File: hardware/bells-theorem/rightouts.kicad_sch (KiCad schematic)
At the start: 54 parts, among them U4 TL074, U5 TL074, U6 TL074, U7 TL072

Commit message: Modified with Jim M's recommendations for input scaling
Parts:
- C10, C11, C12, C13, C7, C8, C9: value 15nF -> 1nF
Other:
- note added: "PWM single pole RC filters 10K + 1nF for 15KHz cutoff (PWM output at 146KHz)"
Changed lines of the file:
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@@
     (stroke (width 0) (type default) (color 0 0 0 0))
+  )
+  (text "PWM single pole RC filters\n10K + 1nF for 15KHz cutoff\n(PWM output at 146KHz)"
+    (at 151.13 90.805 0)
+    (effects (font (size 1.27 1.27)) (justify left bottom))
   )
   (hierarchical_label "ABC_in" (shape input) (at 59.69 77.47 180)
@@
       (effects (font (size 1.27 1.27)) (justify left))
     )
-    (property "Value" "15nF" (id 1) (at 78.74 167.64 90)
+    (property "Value" "1nF" (id 1) (at 78.74 167.64 90)
       (effects (font (size 1.27 1.27)) (justify left))
     )
@@
       (effects (font (size 1.27 1.27)) (justify left))
     )
-    (property "Value" "15nF" (id 1) (at 77.47 139.7 90)
+    (property "Value" "1nF" (id 1) (at 77.47 139.7 90)
       (effects (font (size 1.27 1.27)) (justify left))
     )
@@
       (effects (font (size 1.27 1.27)) (justify left))
     )
-    (property "Value" "15nF" (id 1) (at 76.2 115.57 90)
+    (property "Value" "1nF" (id 1) (at 76.2 115.57 90)
       (effects (font (size 1.27 1.27)) (justify left))
     )
@@
       (effects (font (size 1.27 1.27)) (justify left))
     )
-    (property "Value" "15nF" (id 1) (at 76.2 88.9 90)
+    (property "Value" "1nF" (id 1) (at 76.2 88.9 90)
       (effects (font (size 1.27 1.27)) (justify left))
     )
@@
       (effects (font (size 1.27 1.27)) (justify left))
     )
-    (property "Value" "15nF" (id 1) (at 74.93 63.5 90)
+    (property "Value" "1nF" (id 1) (at 74.93 63.5 90)
       (effects (font (size 1.27 1.27)) (justify left))
     )
@@
       (effects (font (size 1.27 1.27)) (justify left))
     )
-    (property "Value" "15nF" (id 1) (at 76.2 39.37 90)
+    (property "Value" "1nF" (id 1) (at 76.2 39.37 90)
       (effects (font (size 1.27 1.27)) (justify left))
     )
@@
       (effects (font (size 1.27 1.27)) (justify left))
     )
-    (property "Value" "15nF" (id 1) (at 74.93 13.97 90)
-      (effects (font (size 1.27 1.27)) (justify left))
-    )
+    (property "Value" "1nF" (id 1) (at 74.93 13.97 90)
+      (effects (font (size 1.27 1.27)) (justify left))
+    )

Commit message: All changes up to date with latest revisions
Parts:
- C10, C11, C12, C13, C14, C15, C16, C17, C18, C19, C20, C21, C7, C8, C9: footprint Capacitor_SMD:C_0805_2012Metric_Pad1.15x1.40mm_HandSolder -> Capacitor_SMD:C_0805_2012Metric_Pad1.18x1.45mm_HandSolder
- R11, R14, R17, R20, R23, R26, R29, R32, R35, R36, R37, R38, R39, R40, R41, R42, R43, R44, R45, R46, R47, R48, R49, R50, R51, R52, R53, R54, R55, R56, R57, R58, R59, R60, R61: footprint Resistor_SMD:R_0805_2012Metric_Pad1.15x1.40mm_HandSolder -> Resistor_SMD:R_0805_2012Metric_Pad1.20x1.40mm_HandSolder
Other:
- title: (none) -> Bell's Theorem

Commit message: last hardware / software updates
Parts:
- removed C15, C17, C19, C21: 100nF, Capacitor_SMD:C_0805_2012Metric_Pad1.18x1.45mm_HandSolder, symbol Device:C_Small
- added C62, C63, C64, C65, C66, C67, C68: 2n, Capacitor_SMD:C_0805_2012Metric_Pad1.18x1.45mm_HandSolder, symbol Device:C_Small
- C10, C11, C12, C13, C7, C8, C9: value 1nF -> 3.3n
- U4, U5, U6: symbol Amplifier_Operational:TL074 -> Amplifier_Operational:MCP6004
- U7: symbol Amplifier_Operational:TL072 -> Amplifier_Operational:MCP6002-xSN
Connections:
- net -12V is gone; now on net GND: U4.11 (V-), U5.11 (V-), U6.11 (V-), U7.4 (V-)
- net AB: now also C65.1
- net ABC: now also C66.1
- net ABCD: now also C68.1
- net B: now also C64.1
- net BC: now also C63.1
- net BCD: now also C67.1
- net C: now also C62.1
- net at R41.1, R48.2, U4.2 (-): now also C64.2
- net at R42.1, R51.2, U4.6 (-): now also C65.2
- net at R47.1, R54.2, U7.2 (-): now also C68.2
- net at R43.1, R49.2, U5.2 (-): now also C66.2
- net at R44.1, R52.2, U5.6 (-): now also C63.2
- net at R45.1, R50.2, U6.2 (-): now also C67.2
- net at R46.1, R53.2, U6.6 (-): now also C62.2
- net +12V renamed +10V
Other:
- note added: "symbols are changed but the freaking names are not"
- note removed: "PWM single pole RC filters 10K + 1nF for 15KHz cutoff (PWM output at 146KHz)"
- moved on the sheet: R14, R20, R26

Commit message: version 0.6 hardware and code
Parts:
- added C21, C35, C37, C39: 100nF, Capacitor_SMD:C_0805_2012Metric_Pad1.18x1.45mm_HandSolder, symbol Device:C_Small
- U4, U5, U6: value TL074 -> TLV9304; symbol Amplifier_Operational:MCP6004 -> Amplifier_Operational:TLC274
- U7: value TL072 -> TLV9302; symbol Amplifier_Operational:MCP6002-xSN -> Amplifier_Operational:TLC272
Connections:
- net GND: now also C21.2, C35.2, C37.2, C39.2; no longer U4.11 (V-), U5.11 (V-), U6.11 (V-), U7.4 (V-)
- new net -10V: C21.1, C35.1, C37.1, C39.1, U4.11 (V-), U5.11 (V-), U6.11 (V-), U7.4 (V-)
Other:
- note added: "Can't use 6004's they won't tolerate 10V operation"
- note added: "doing this architecture with single sided supplies is a lot more complicated than it might look. So using dual supply."
- note removed: "symbols are changed but the freaking names are not"

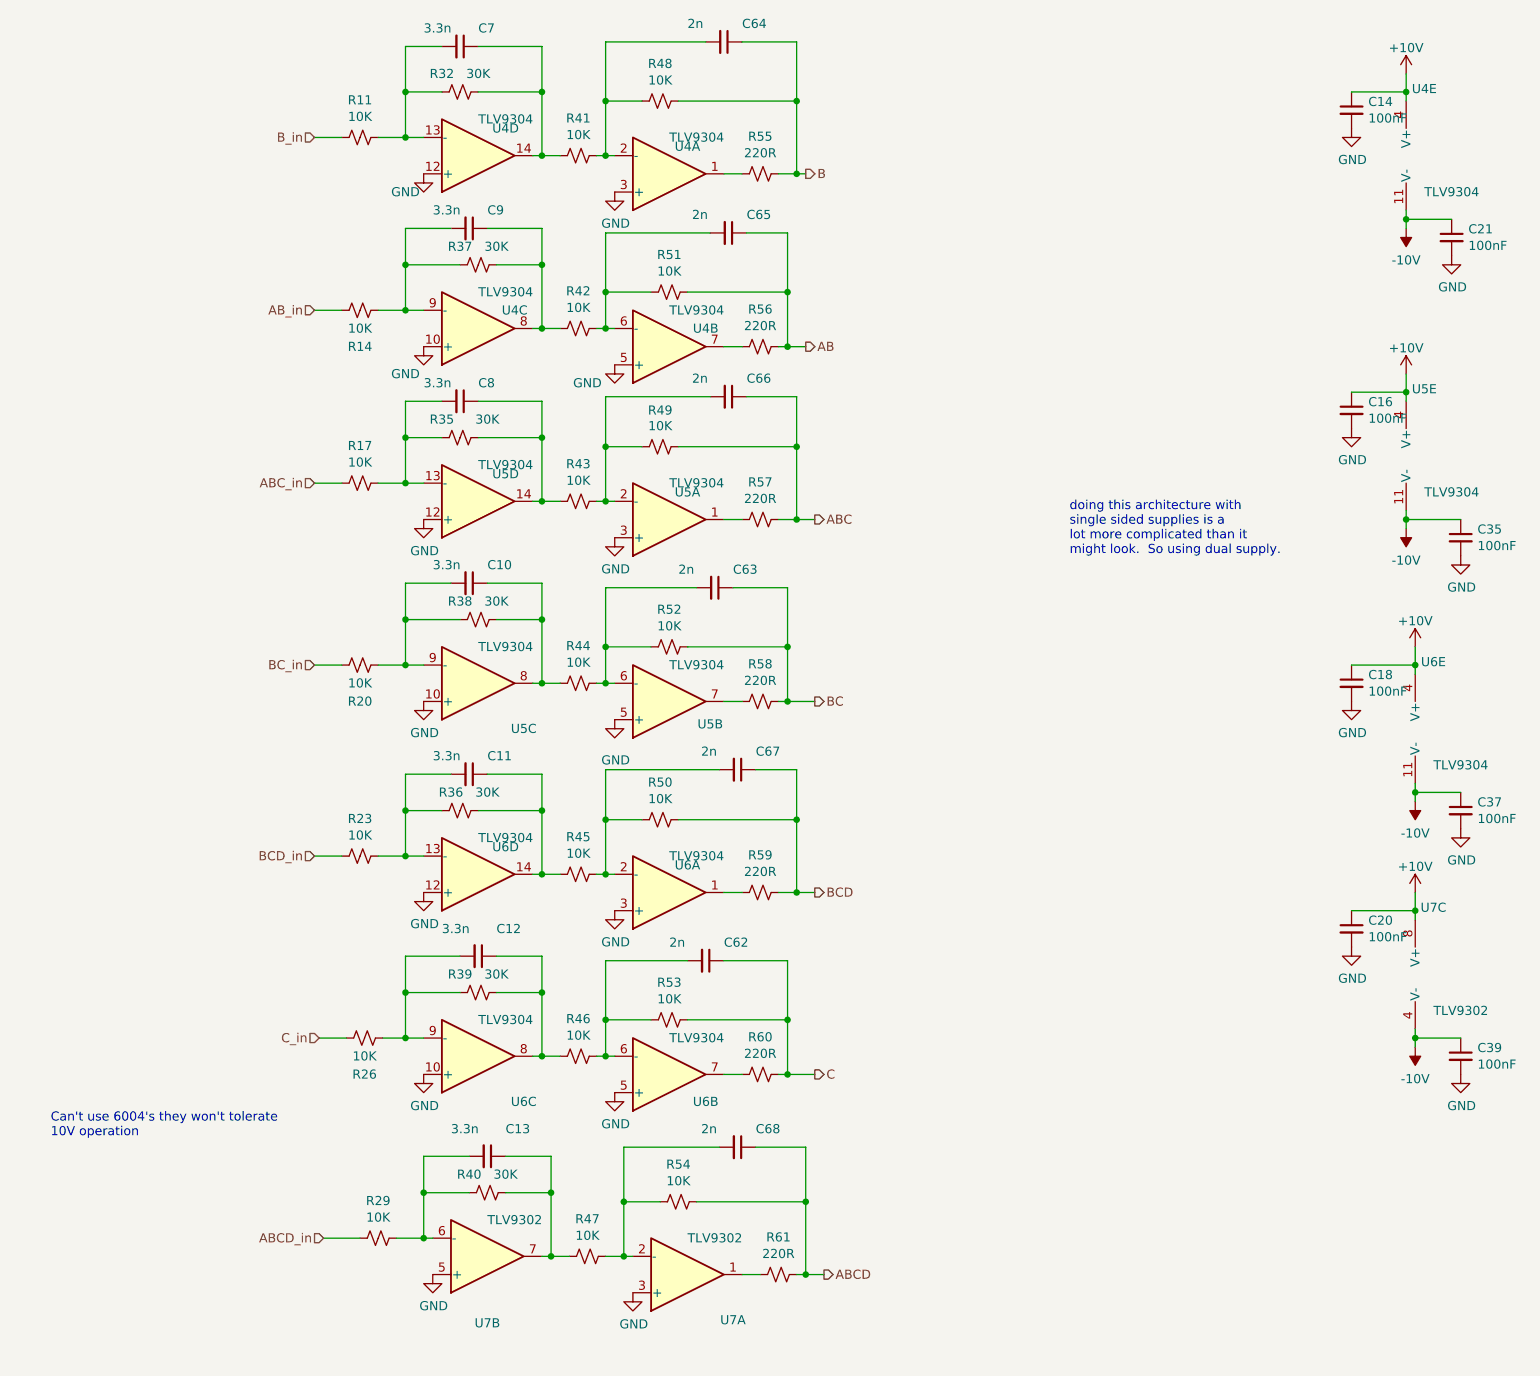
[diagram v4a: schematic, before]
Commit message: current revision actually 0.6 was 1.0 candidate, but needs major revision
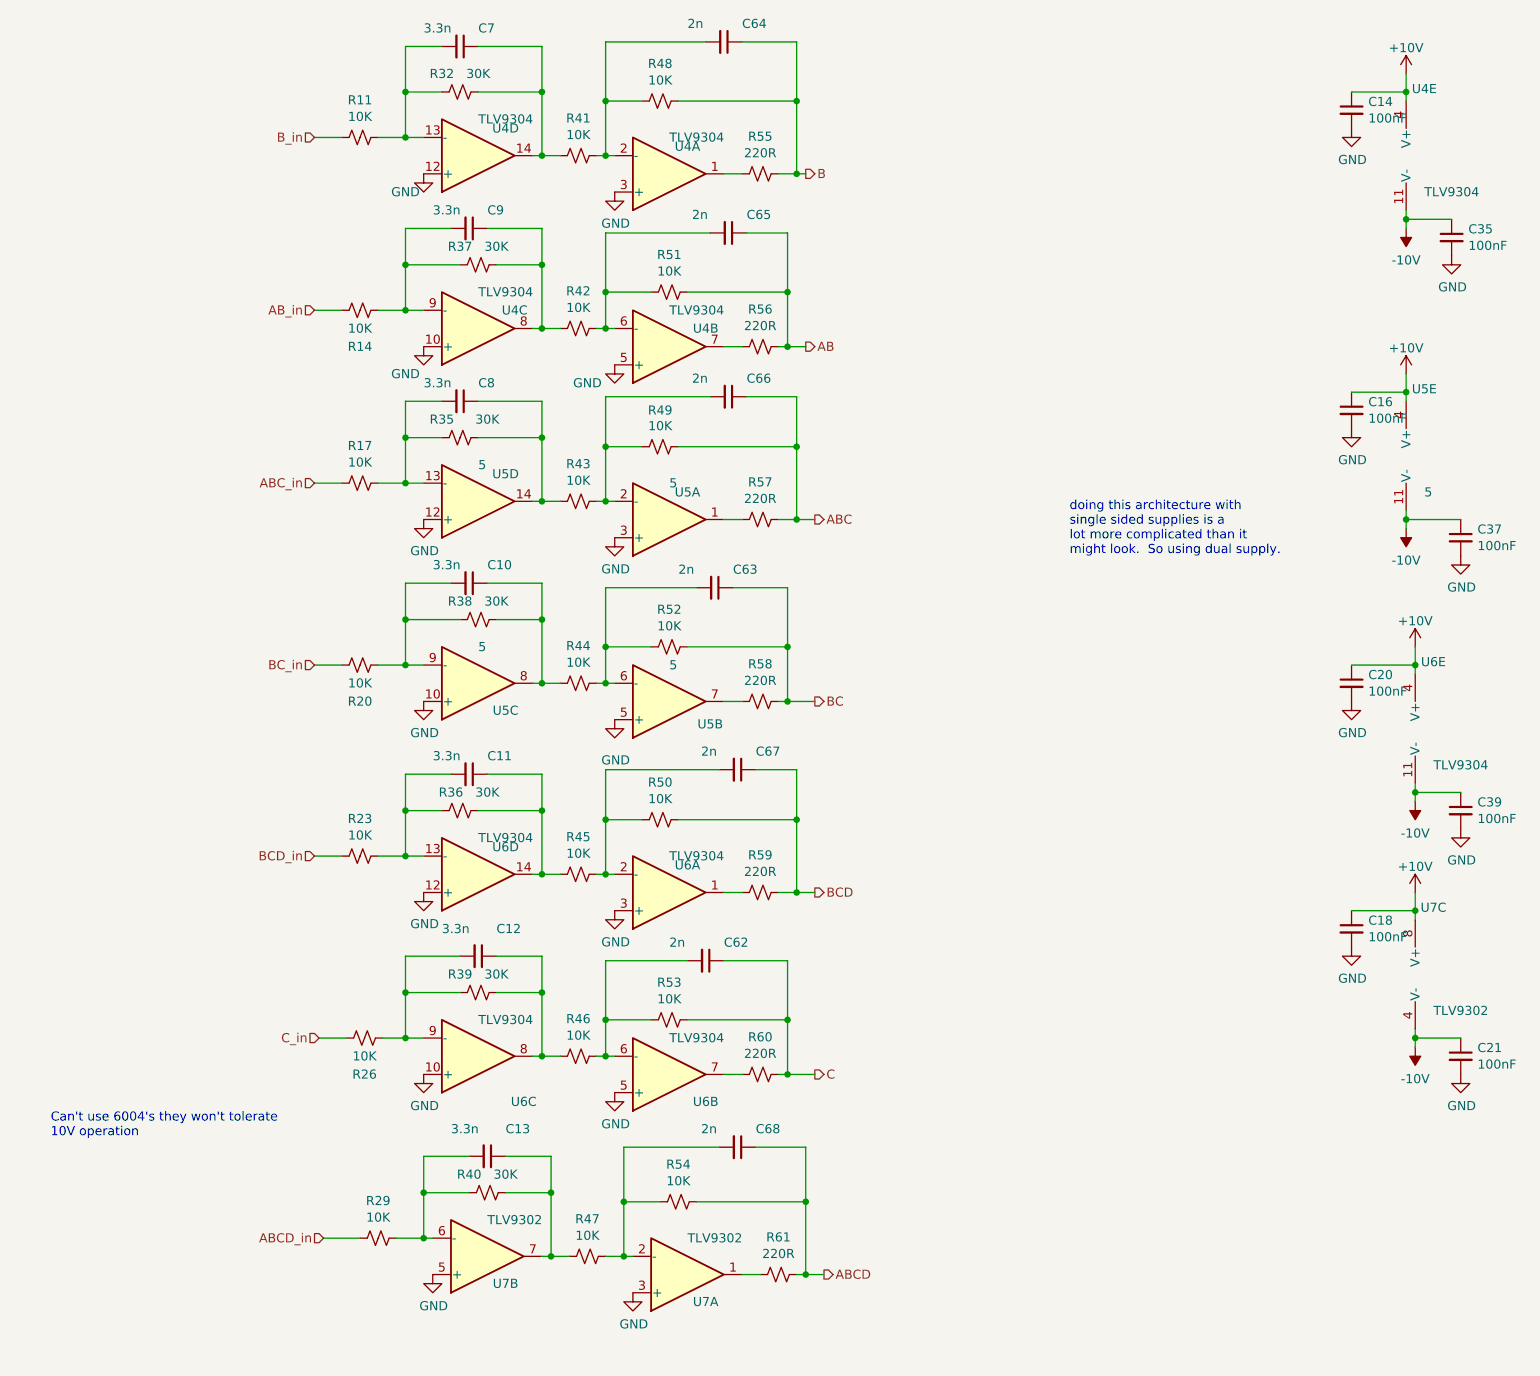
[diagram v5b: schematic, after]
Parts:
- U5: value TLV9304 -> 5
- renumbered C20 to C18, C18 to C20, C39 to C21, C21 to C35, C35 to C37, C37 to C39

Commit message: checking in old outstanding changes prior to debugging with Claude Code
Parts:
- added R122, R123, R124, R125, R126, R127, R131: 30K, Resistor_SMD:R_0805_2012Metric_Pad1.20x1.40mm_HandSolder, symbol Device:R_Small_US
- added R133, R134, R137, R138, R139, R140, R141: 10K, Resistor_SMD:R_0805_2012Metric_Pad1.20x1.40mm_HandSolder, symbol Device:R_Small_US
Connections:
- net GND: now also R133.2, R134.2, R137.2, R138.2, R139.2, R140.2, R141.2; no longer U4.10 (+), U4.12 (+), U5.10 (+), U5.12 (+), U6.10 (+), U6.12 (+), U7.5 (+)
- net +10V renamed +12V
- net -10V renamed -12V
- new net: R122.1, R133.1, U4.12 (+)
- new net: R123.1, R134.1, U4.10 (+)
- new net: R131.1, R141.1, U7.5 (+)
- new net: R124.1, R137.1, U5.12 (+)
- new net: R125.1, R138.1, U5.10 (+)
- new net: R126.1, R139.1, U6.12 (+)
- new net: R127.1, R140.1, U6.10 (+)
- new net +5V: R122.2, R123.2, R124.2, R125.2, R126.2, R127.2, R131.2
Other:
- note added: "NEED TO VALIDATE in another circuit I calculated the input impedance on the + side as Rin || Rgnd which in this case would be 7.5K If that's correct, then the 5/3 V offset is being multiplied by 4."
- note added: "as shown, gives -5V to +5V output alternately, omit 30K on the + input, and tie directly to ground with 0R in place of the 10K to ground to get 0 - 10V output"
- note removed: "Can't use 6004's they won't tolerate 10V operation"
- note removed: "doing this architecture with single sided supplies is a lot more complicated than it might look. So using dual supply."
